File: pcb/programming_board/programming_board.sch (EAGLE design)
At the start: 28 parts, among them IC1 4053D, IC2 74ABT125PW

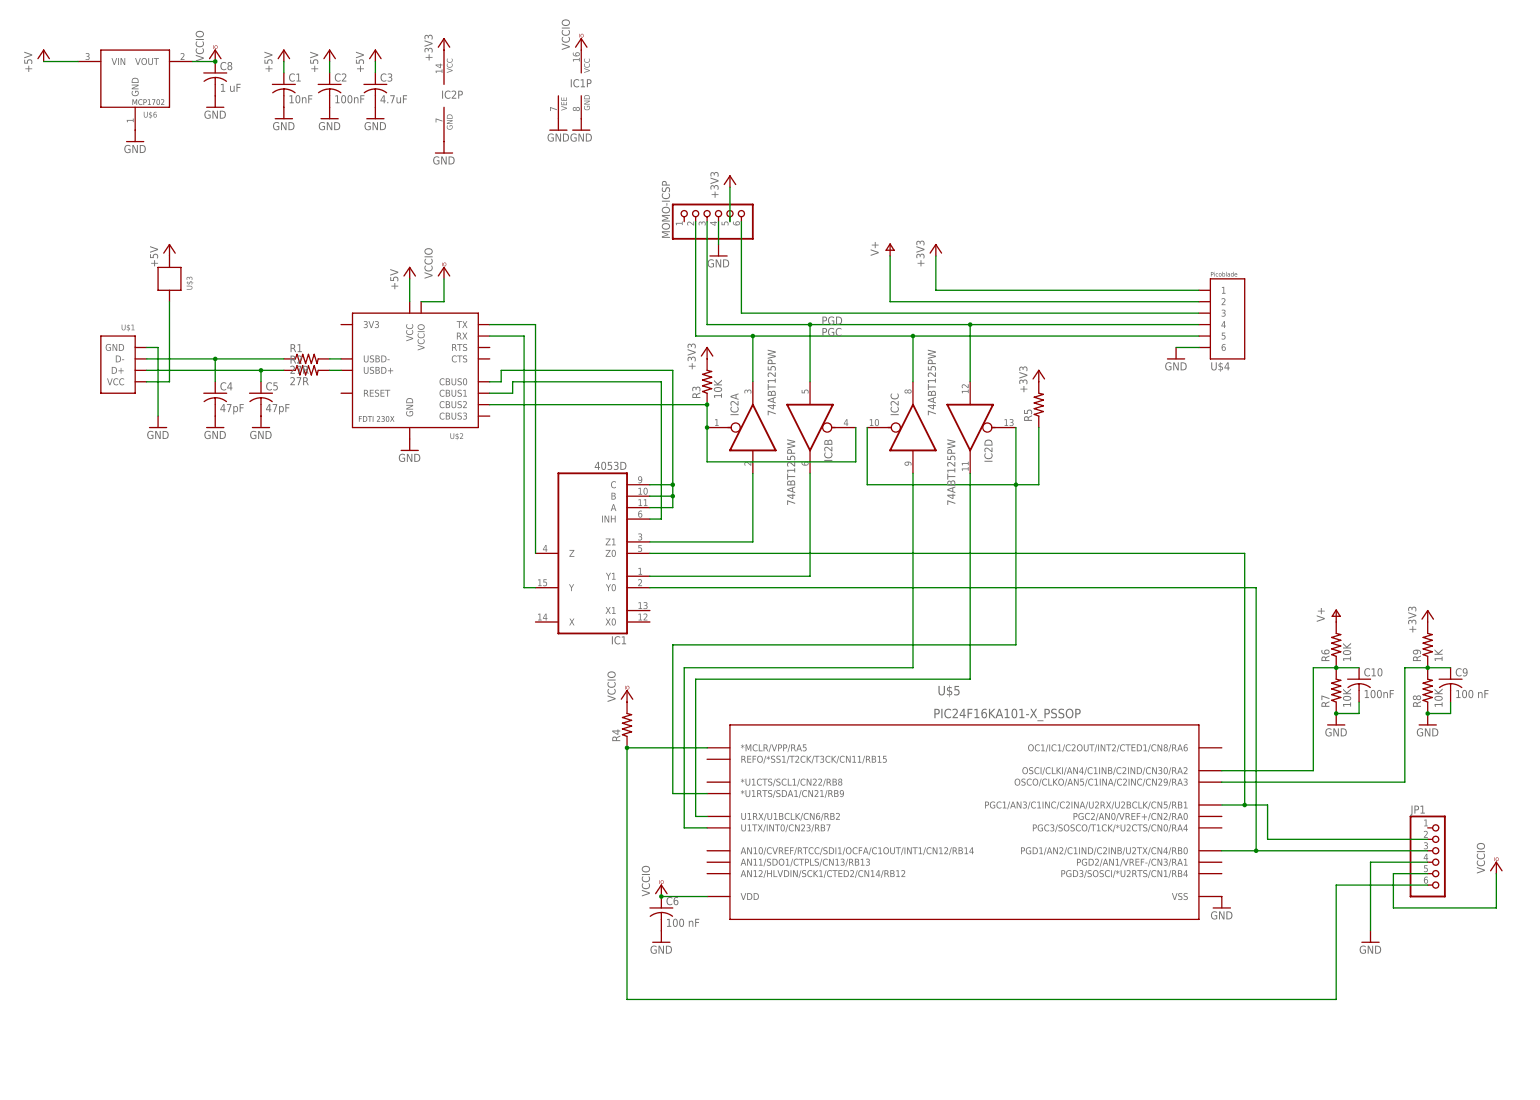
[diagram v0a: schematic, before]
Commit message: Laid out first complete version of pcb
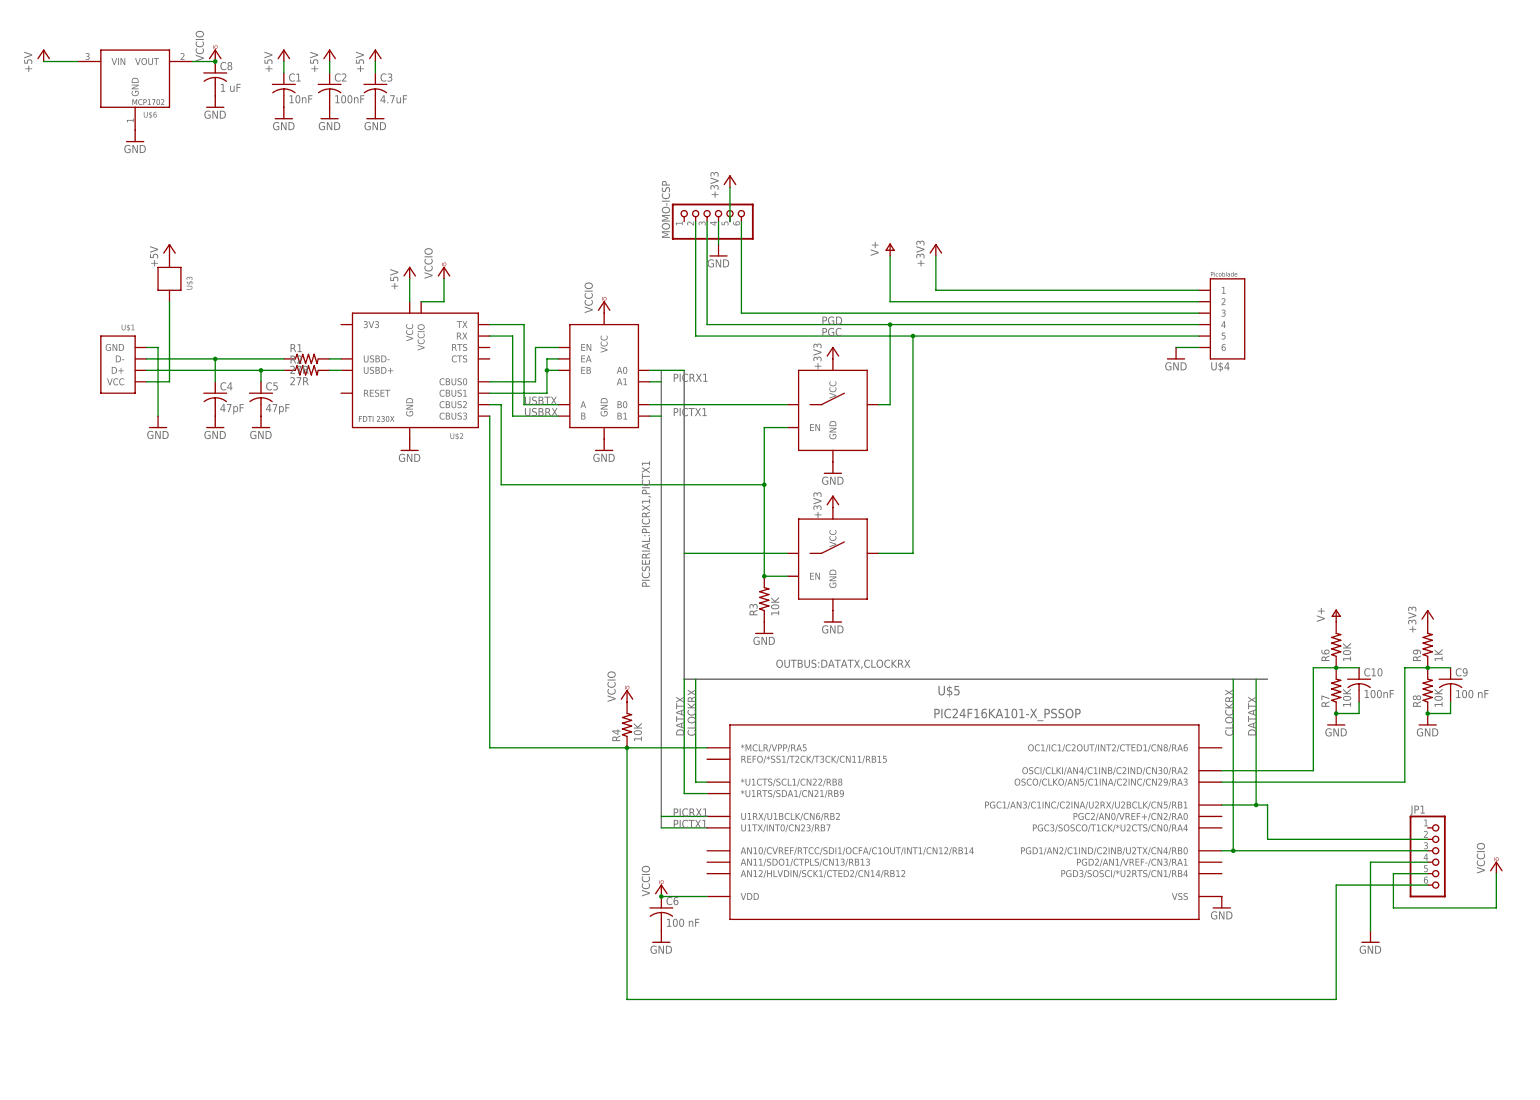
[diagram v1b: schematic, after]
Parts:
- removed IC1: 4053D, 40xx:4053D
- removed IC2: 74ABT125PW, 74xx-us:74ABT125PW
- removed R5: (no value), rcl:R-US_R0603
- added U$7: DG636, components:DG636
- added U$8, U$9: TS5A1066-SPST, components:TS5A1066-SPST
- R4: value (none) -> 10K
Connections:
- removed net N$12: IC1A.Y1, IC2B.O
- removed net N$13: IC1A.Z1, IC2A.I
- removed net N$14: IC2C.I, U$5.U1TX/INT0/CN23/RB7
- removed net N$15: IC2D.O, U$5.U1RX/U1BCLK/CN6/RB2
- removed net N$16: IC2C.OE, IC2D.OE, R5.1, U$5.*U1RTS/SDA1/CN21/RB9
- removed net N$18: IC1A.Z0, JP1.2, U$5.PGC1/AN3/C1INC/C2INA/U2RX/U2BCLK/CN5/RB1
- removed net N$19: IC1A.Y0, JP1.3, U$5.PGD1/AN2/C1IND/C2INB/U2TX/CN4/RB0
- removed net N$8: IC1A.Y, U$2.RX
- removed net N$9: IC1A.A, IC1A.B, IC1A.C, U$2.CBUS0
- new net CLOCKRX: JP1.3, U$5.*U1CTS/SCL1/CN22/RB8, U$5.PGD1/AN2/C1IND/C2INB/U2TX/CN4/RB0, U$7.A0, U$9.COM
- new net DATATX: JP1.2, U$5.*U1RTS/SDA1/CN21/RB9, U$5.PGC1/AN3/C1INC/C2INA/U2RX/U2BCLK/CN5/RB1, U$7.B0, U$8.COM
- new net PICRX1: U$5.U1RX/U1BCLK/CN6/RB2, U$7.A1
- new net PICTX1: U$5.U1TX/INT0/CN23/RB7, U$7.B1
- new net USBRX: U$2.RX, U$7.B
- new net USBTX: U$2.TX, U$7.A
- net +3V3: now also U$8.VCC, U$9.VCC; no longer IC2P.VCC, R3.2, R5.2
- net GND: now also R3.1, U$7.GND, U$8.GND, U$9.GND; no longer IC1P.GND, IC1P.VEE, IC2P.GND
- net N$10: now also U$2.CBUS0, U$7.EN; no longer IC2A.OE, IC2B.OE, R3.1, U$2.CBUS2
- net N$11: now also U$7.EA, U$7.EB; no longer IC1A.INH
- net N$21: now also U$2.CBUS3
- net N$7: now also R3.2, U$2.CBUS2, U$9.EN; no longer IC1A.Z, U$2.TX
- net PGC: now also U$9.NO; no longer IC2A.O, IC2C.O
- net PGD: now also U$8.NO; no longer IC2B.I, IC2D.I
- net VCCIO: now also U$7.VCC; no longer IC1P.VCC
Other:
- moved on the sheet: R3

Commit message: Finished programming board (Momo Field Service Unit)
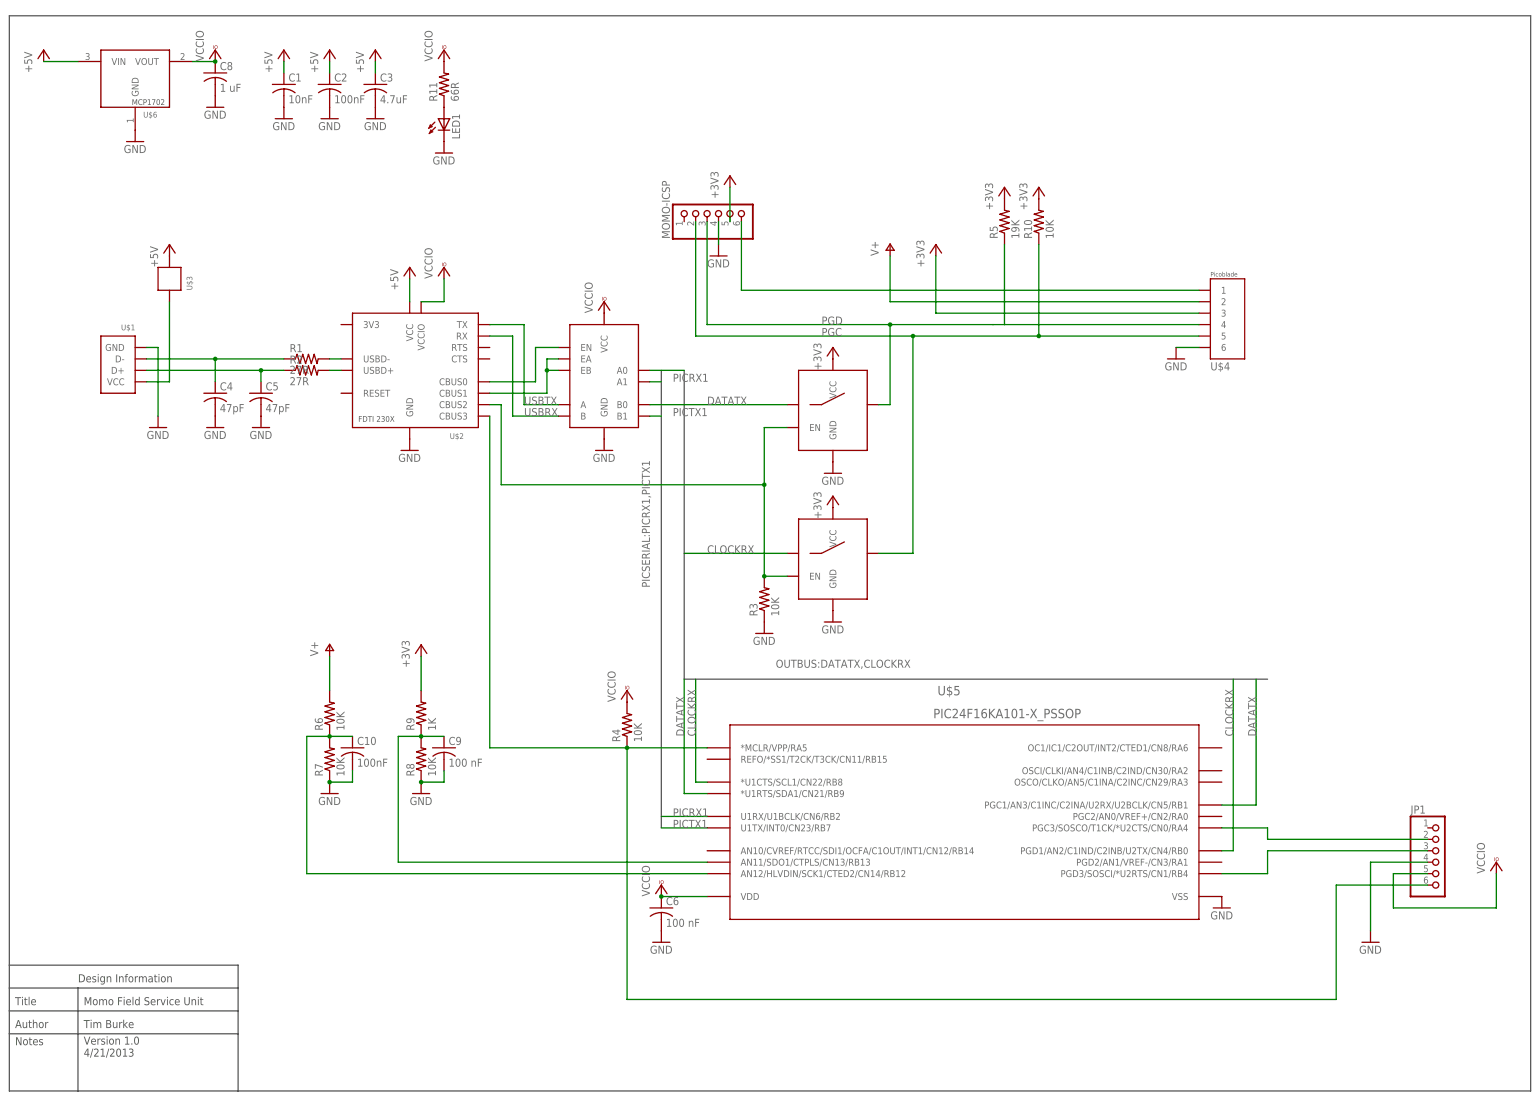
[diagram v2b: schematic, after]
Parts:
- added LED1: (no value), led:LED5MM
- added R10: 10K, rcl:R-US_R0603
- added R11: 66R, rcl:R-US_R0603
- added R5: 19K, rcl:R-US_R0603
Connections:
- new net N$12: LED1.A, R11.1
- new net N$8: JP1.2, U$5.PGC3/SOSCO/T1CK/*U2CTS/CN0/RA4
- new net N$9: JP1.3, U$5.PGD3/SOSCI/*U2RTS/CN1/RB4
- net +3V3: now also R10.2, R5.2, U$4.3; no longer U$4.1
- net CLOCKRX: no longer JP1.3
- net DATATX: no longer JP1.2
- net GND: now also LED1.C
- net N$17: now also U$5.AN12/HLVDIN/SCK1/CTED2/CN14/RB12; no longer U$5.OSCI/CLKI/AN4/C1INB/C2IND/CN30/RA2
- net N$20: now also U$5.AN11/SDO1/CTPLS/CN13/RB13; no longer U$5.OSCO/CLKO/AN5/C1INA/C2INC/CN29/RA3
- net N$6: now also U$4.1; no longer U$4.3
- net N$7: now also U$8.EN
- net PGC: now also R10.1
- net PGD: now also R5.1
- net VCCIO: now also R11.2
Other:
- note added: "Author"
- note added: "Design Information"
- note added: "Momo Field Service Unit"
- note added: "Notes"
- note added: "Tim Burke"
- note added: "Title"
- note added: "Version 1.0 4/21/2013"
- moved on the sheet: C10, C9, R6, R7, R8, R9

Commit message: Final version 1.0 of the programming board
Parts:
- added LED2: (no value), led:LED5MM
- added R12: 66R, rcl:R-US_R0603
- R5: value 19K -> 10K
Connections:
- new net N$13: LED2.A, R12.1
- net +3V3: now also R12.2
- net GND: now also LED2.C
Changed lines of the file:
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@@
 <part name="+3V5" library="supply1" deviceset="+3V3" device=""/>
 <part name="GND15" library="supply1" deviceset="GND" device=""/>
-<part name="R5" library="rcl" deviceset="R-US_" device="R0603" value="19K"/>
+<part name="R5" library="rcl" deviceset="R-US_" device="R0603" value="10K"/>
 <part name="R10" library="rcl" deviceset="R-US_" device="R0603" value="10K"/>
 <part name="+3V6" library="supply1" deviceset="+3V3" device=""/>
@@
 <part name="GND20" library="supply1" deviceset="GND" device=""/>
 <part name="VCC7" library="supply1" deviceset="VCCIO" device=""/>
+<part name="LED2" library="led" deviceset="LED" device="5MM"/>
+<part name="R12" library="rcl" deviceset="R-US_" device="R0603" value="66R"/>
+<part name="+3V8" library="supply1" deviceset="+3V3" device=""/>
+<part name="GND22" library="supply1" deviceset="GND" device=""/>
 </parts>
 <sheets>
@@
 <instance part="GND20" gate="1" x="81.28" y="96.52"/>
 <instance part="VCC7" gate="G$1" x="81.28" y="119.38"/>
+<instance part="LED2" gate="G$1" x="93.98" y="104.14"/>
+<instance part="R12" gate="G$1" x="93.98" y="111.76" rot="R90"/>
+<instance part="+3V8" gate="G$1" x="93.98" y="119.38"/>
+<instance part="GND22" gate="1" x="93.98" y="96.52"/>
 </instances>
 <busses>
@@
 <pinref part="LED1" gate="G$1" pin="C"/>
 <pinref part="GND20" gate="1" pin="GND"/>
+</segment>
+<segment>
+<pinref part="LED2" gate="G$1" pin="C"/>
+<pinref part="GND22" gate="1" pin="GND"/>
 </segment>
 </net>
@@
 <pinref part="R10" gate="G$1" pin="2"/>
 <pinref part="+3V7" gate="G$1" pin="+3V3"/>
+</segment>
+<segment>
+<pinref part="R12" gate="G$1" pin="2"/>
+<pinref part="+3V8" gate="G$1" pin="+3V3"/>
 </segment>
 </net>
@@
 </segment>
 </net>
+<net name="N$13" class="0">
+<segment>
+<pinref part="LED2" gate="G$1" pin="A"/>
+<pinref part="R12" gate="G$1" pin="1"/>
+</segment>
+</net>
